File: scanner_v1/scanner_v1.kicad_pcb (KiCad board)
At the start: 2 copper layers, 39 parts, among them J1 USB_B, Q1 SS8050, Q2 SS8050, Q3 2N3906, Q4 SS8050, Q5 SS8050, U1 LM321, U2 TS2431BILT, U3 LM321, U4 PIC16F84A-XXSO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

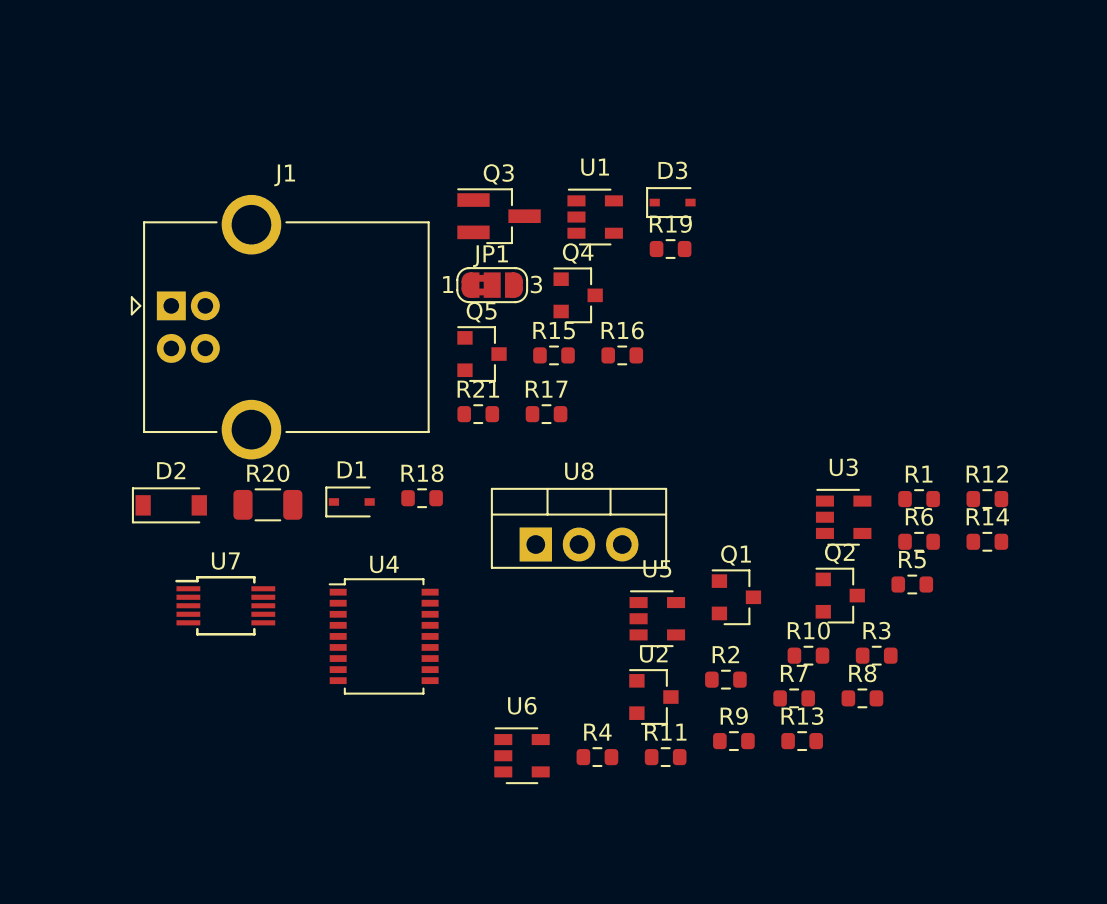
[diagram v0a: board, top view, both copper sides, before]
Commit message: added ISO/VPW/PWM receivers
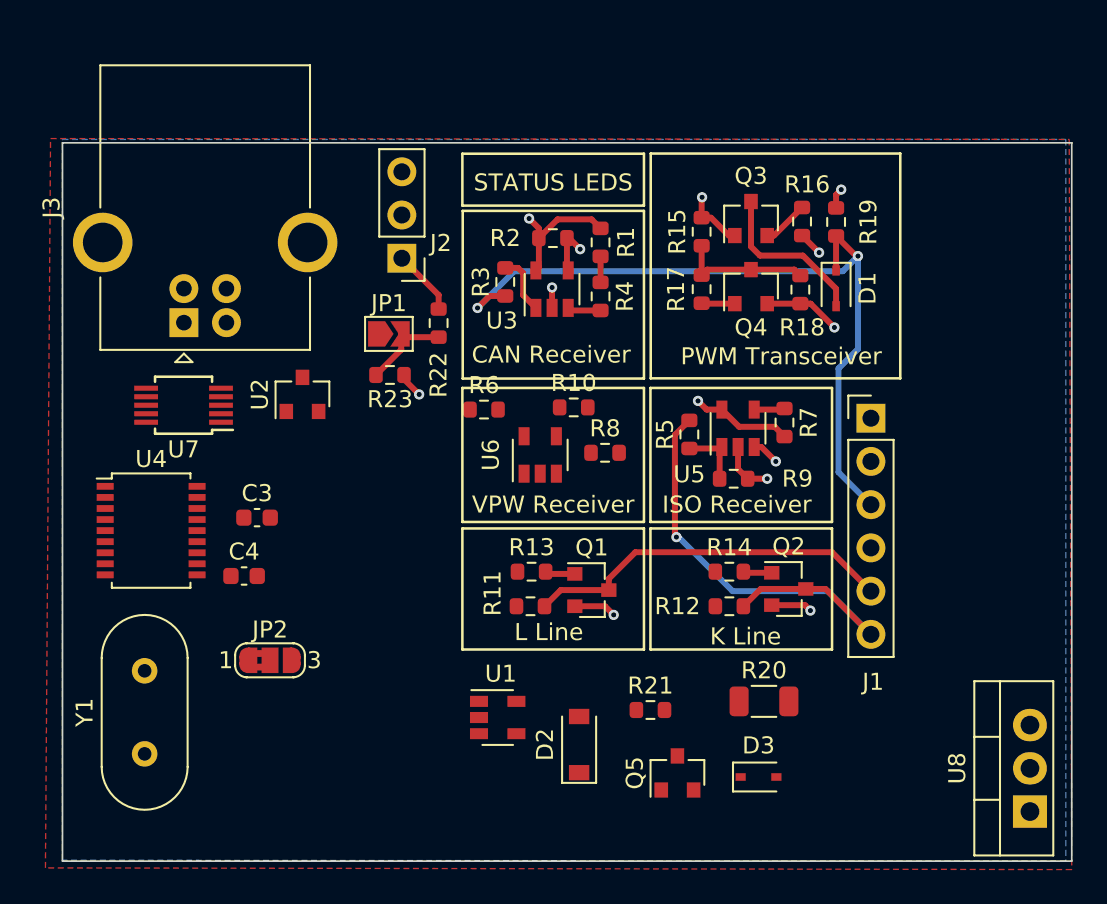
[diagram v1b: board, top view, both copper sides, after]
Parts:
- added C3: 20pF, Capacitor_SMD:C_0603_1608Metric, F.Cu at (124.3, 117.2)
- added C4: 20pF, Capacitor_SMD:C_0603_1608Metric, F.Cu at (123.6, 120.7)
- added J2: Conn_01x03, Connector_PinHeader_2.54mm:PinHeader_1x03_P2.54mm_Vertical, F.Cu at (132.8, 102.0)
- added J3: USB_B, Connector_USB:USB_B_OST_USB-B1HSxx_Horizontal, F.Cu at (120.0, 105.8)
- added JP2: Jumper_3_Bridged12, Jumper:SolderJumper-3_P1.3mm_Bridged2Bar12_RoundedPad1.0x1.5mm_NumberLabels, F.Cu at (125.1, 125.6)
- added R22: 10k, Resistor_SMD:R_0603_1608Metric, F.Cu at (135.0, 105.8)
- added R23: 10k, Resistor_SMD:R_0603_1608Metric, F.Cu at (132.1, 108.8)
- added Y1: 20Mhz, Crystal:Crystal_HC49-4H_Vertical, F.Cu at (117.7, 131.1)
- J1: value USB_B -> Conn_01x06; footprint Connector_USB:USB_B_OST_USB-B1HSxx_Horizontal -> Connector_PinHeader_2.54mm:PinHeader_1x06_P2.54mm_Vertical
- JP1: value Jumper_3_Bridged12 -> DB9; footprint Jumper:SolderJumper-3_P1.3mm_Bridged2Bar12_RoundedPad1.0x1.5mm_NumberLabels -> Jumper:SolderJumper-2_P1.3mm_Open_TrianglePad1.0x1.5mm
- Q3: footprint Package_TO_SOT_SMD:SOT-23_Handsoldering -> Package_TO_SOT_SMD:SOT-23
- moved J1 41.6 mm to (160.4, 111.4)
- moved D3 34.1 mm to (153.8, 132.5)
- moved U8 33.0 mm to (169.7, 134.5), turned to 90 degrees
- moved R20 31.4 mm to (154.1, 128.0)
- moved D1 31.1 mm to (158.4, 103.7), turned to -90 degrees
- moved R3 31.0 mm to (138.9, 103.4), turned to 90 degrees
- moved U1 30.0 mm to (138.5, 129.0)
- moved R2 27.9 mm to (141.7, 100.8), turned to 180 degrees
- moved D2 27.8 mm to (143.3, 130.6), turned to 90 degrees
- moved U2 27.2 mm to (127.0, 110.0), turned to 90 degrees
- moved Q5 27.2 mm to (149.0, 132.2), turned to 90 degrees
- moved R4 27.1 mm to (144.5, 104.2), turned to -90 degrees
- moved R6 26.7 mm to (137.7, 110.9)
- moved R18 25.4 mm to (156.3, 103.8), turned to 90 degrees
- moved R1 24.0 mm to (144.5, 101.0), turned to 90 degrees
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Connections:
- J1 pad 1: /VBUS -> +12V
- J1 pad 2: /USB_D- -> GND
- J1 pad 3: /USB_D+ -> /CAN+
- J1 pad 4: GND -> /CAN-
- J1 pad 5: GND -> /L_Line
- JP1 pad 1: /VBUS -> /xTXD
- JP1 pad 2: +5V -> Net-(JP1-Pad2)
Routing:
- net /CAN+: track 0.00 -> 45.2 mm, vias 0 -> 2
- net /K_Line: track 0.00 -> 30.1 mm, vias 0 -> 1
- net /L_Line: track 0.00 -> 21.8 mm
- net +5V: track 0.00 -> 17.2 mm, vias 0 -> 3
- net GND: track 0.00 -> 16.6 mm, vias 0 -> 7
- net Net-(D1-Pad2): track 0.00 -> 9.70 mm
- net /xCAN-: track 0.00 -> 7.81 mm
- net Net-(JP1-Pad2): track 0.00 -> 5.30 mm
- net Net-(J2-Pad1): track 0.00 -> 3.88 mm
- net Net-(R5-Pad1): track 0.00 -> 3.86 mm
- net Net-(R3-Pad2): track 0.00 -> 3.53 mm
- net /xCAN: track 0.00 -> 2.98 mm, vias 0 -> 1
- net Net-(Q3-Pad2): track 0.00 -> 2.73 mm
- net Net-(R4-Pad2): track 0.00 -> 1.96 mm
- net Net-(Q4-Pad1): track 0.00 -> 1.96 mm
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- added copper zone on F.Cu, net +5V
- added copper zone on B.Cu, net GND
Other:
- board outline added: 59.3 x 42.2 mm
- board text added: "CAN Receiver"
- board text added: "ISO Receiver"
- board text added: "K Line"
- board text added: "L Line"
- board text added: "PWM Transceiver"
- board text added: "STATUS LEDS"
- board text added: "VPW Receiver"

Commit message: finish v01
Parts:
- added C1: 100nF, Capacitor_SMD:C_0805_2012Metric, F.Cu at (129.2, 126.3)
- added C2: 100nF, Capacitor_SMD:C_0805_2012Metric, F.Cu at (125.6, 107.5)
- moved U8 35.6 mm to (134.4, 130.2)
- moved JP1 18.4 mm to (120.1, 120.4), turned to 90 degrees
- moved R22 17.0 mm to (122.1, 117.0)
- moved J2 16.7 mm to (120.4, 113.2)
- moved R23 15.1 mm to (119.4, 116.9), turned to -90 degrees
- moved D3 11.1 mm to (144.4, 126.5)
- moved U7 10.3 mm to (130.2, 109.4), turned to -90 degrees
- moved U2 9.85 mm to (134.2, 116.7)
- moved JP2 9.78 mm to (133.6, 120.8)
- moved D2 9.05 mm to (152.3, 129.8), turned to 180 degrees
- moved U4 8.56 mm to (126.6, 117.3), turned to -90 degrees
- moved C3 7.30 mm to (128.7, 123.0)
- moved J3 6.78 mm to (126.6, 104.0)
- moved R10 4.98 mm to (138.8, 113.5), turned to 90 degrees
- moved Y1 4.88 mm to (122.5, 130.2), turned to 0 degrees
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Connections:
- U1 pad 5: unconnected-(U1-Pad5) -> +5V
- U4 pad 7: /xVPW_T -> /xVPW_R
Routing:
- net +12V: track 0.00 -> 69.9 mm, vias 0 -> 2
- net /xCAN+: track 1.41 -> 52.9 mm, vias 1 -> 2
- net /xCAN-: track 7.81 -> 51.7 mm, vias 0 -> 2
- net /CAN+: track 45.2 -> 85.1 mm, vias 2 -> 4
- net /xISO: track 1.80 -> 38.4 mm, vias 0 -> 4
- net /xCAN: track 2.98 -> 39.5 mm, vias 1 -> 2
- net +2V5: track 1.62 -> 37.4 mm, vias 1 -> 0
- net GND: track 16.6 -> 50.2 mm, vias 7 -> 16
- net /xK_Line: track 0.00 -> 29.8 mm, vias 0 -> 2
- net /xVPW_T: track 0.00 -> 29.7 mm, vias 0 -> 2
- net /xVPW_R: track 0.00 -> 28.7 mm, vias 0 -> 4
- net +5V: track 17.2 -> 44.9 mm, vias 3 -> 11
- net /CAN-: track 1.52 -> 28.9 mm
- net /VBUS: track 0.00 -> 23.9 mm, vias 0 -> 1
- net /xL_Line: track 0.00 -> 16.9 mm, vias 0 -> 2
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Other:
- board size 59.3 x 42.2 mm -> 45.5 x 38.4 mm
- board text added: "VPW Transceiver"

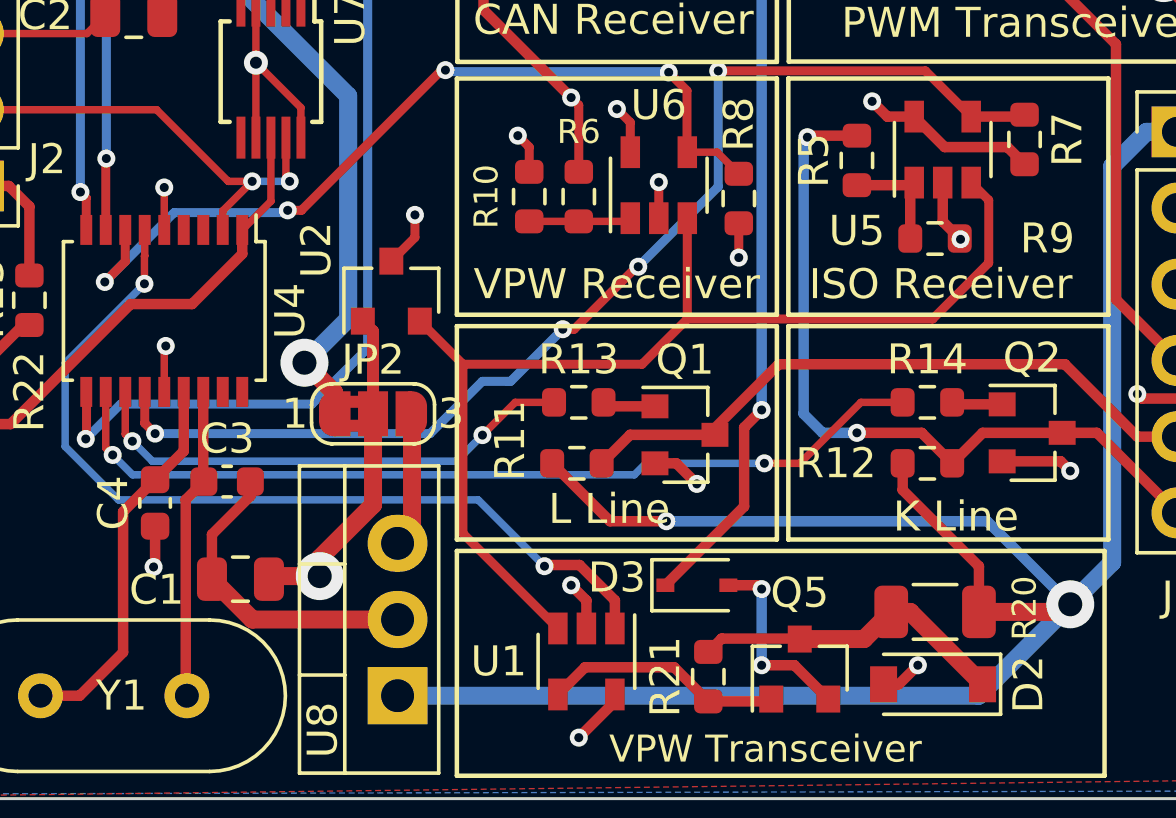
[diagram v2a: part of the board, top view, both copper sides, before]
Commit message: v1, fix on RST pin
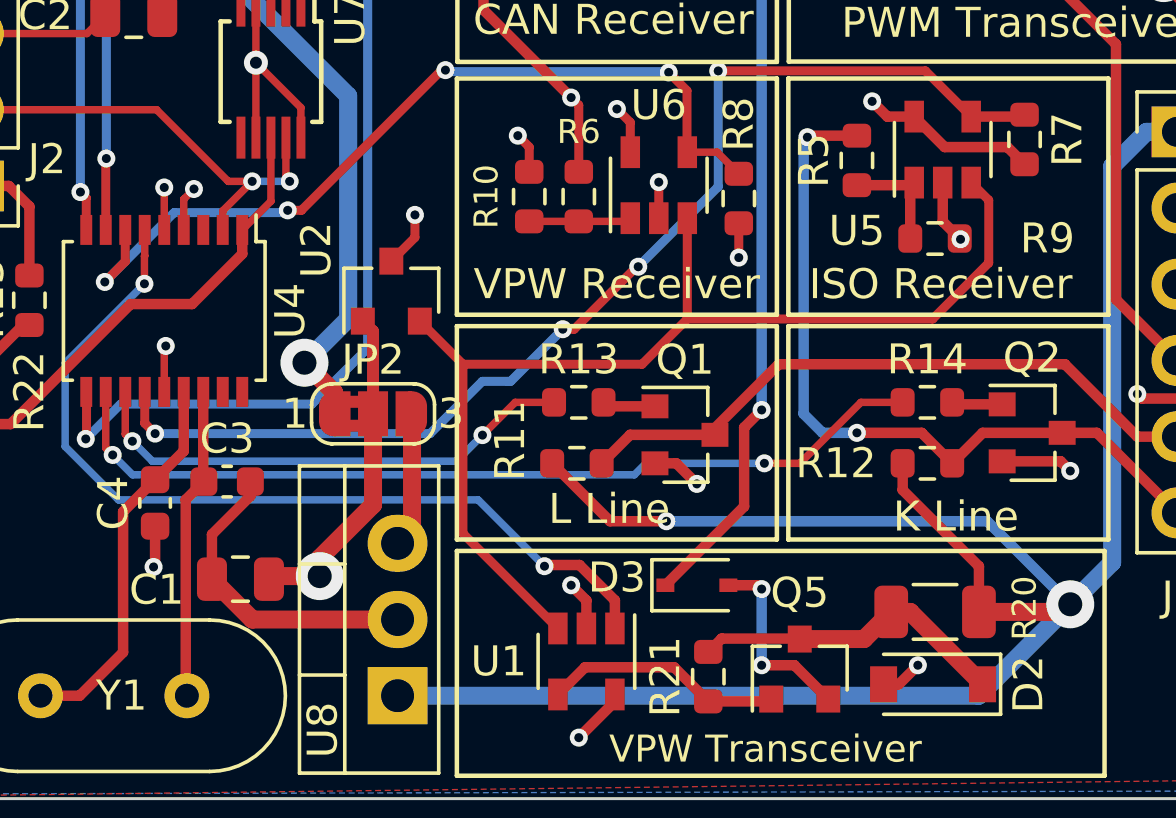
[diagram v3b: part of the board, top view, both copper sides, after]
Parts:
- added Churrosoft: LOGO, logo_lib:churrosoft, B.Cu at (144.9, 115.6)
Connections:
- U4 pad 4: unconnected-(U4-Pad4) -> +5V
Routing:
- net +5V: track 44.9 -> 46.4 mm, vias 11 -> 12
